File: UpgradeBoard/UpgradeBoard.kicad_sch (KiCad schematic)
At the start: 0 parts

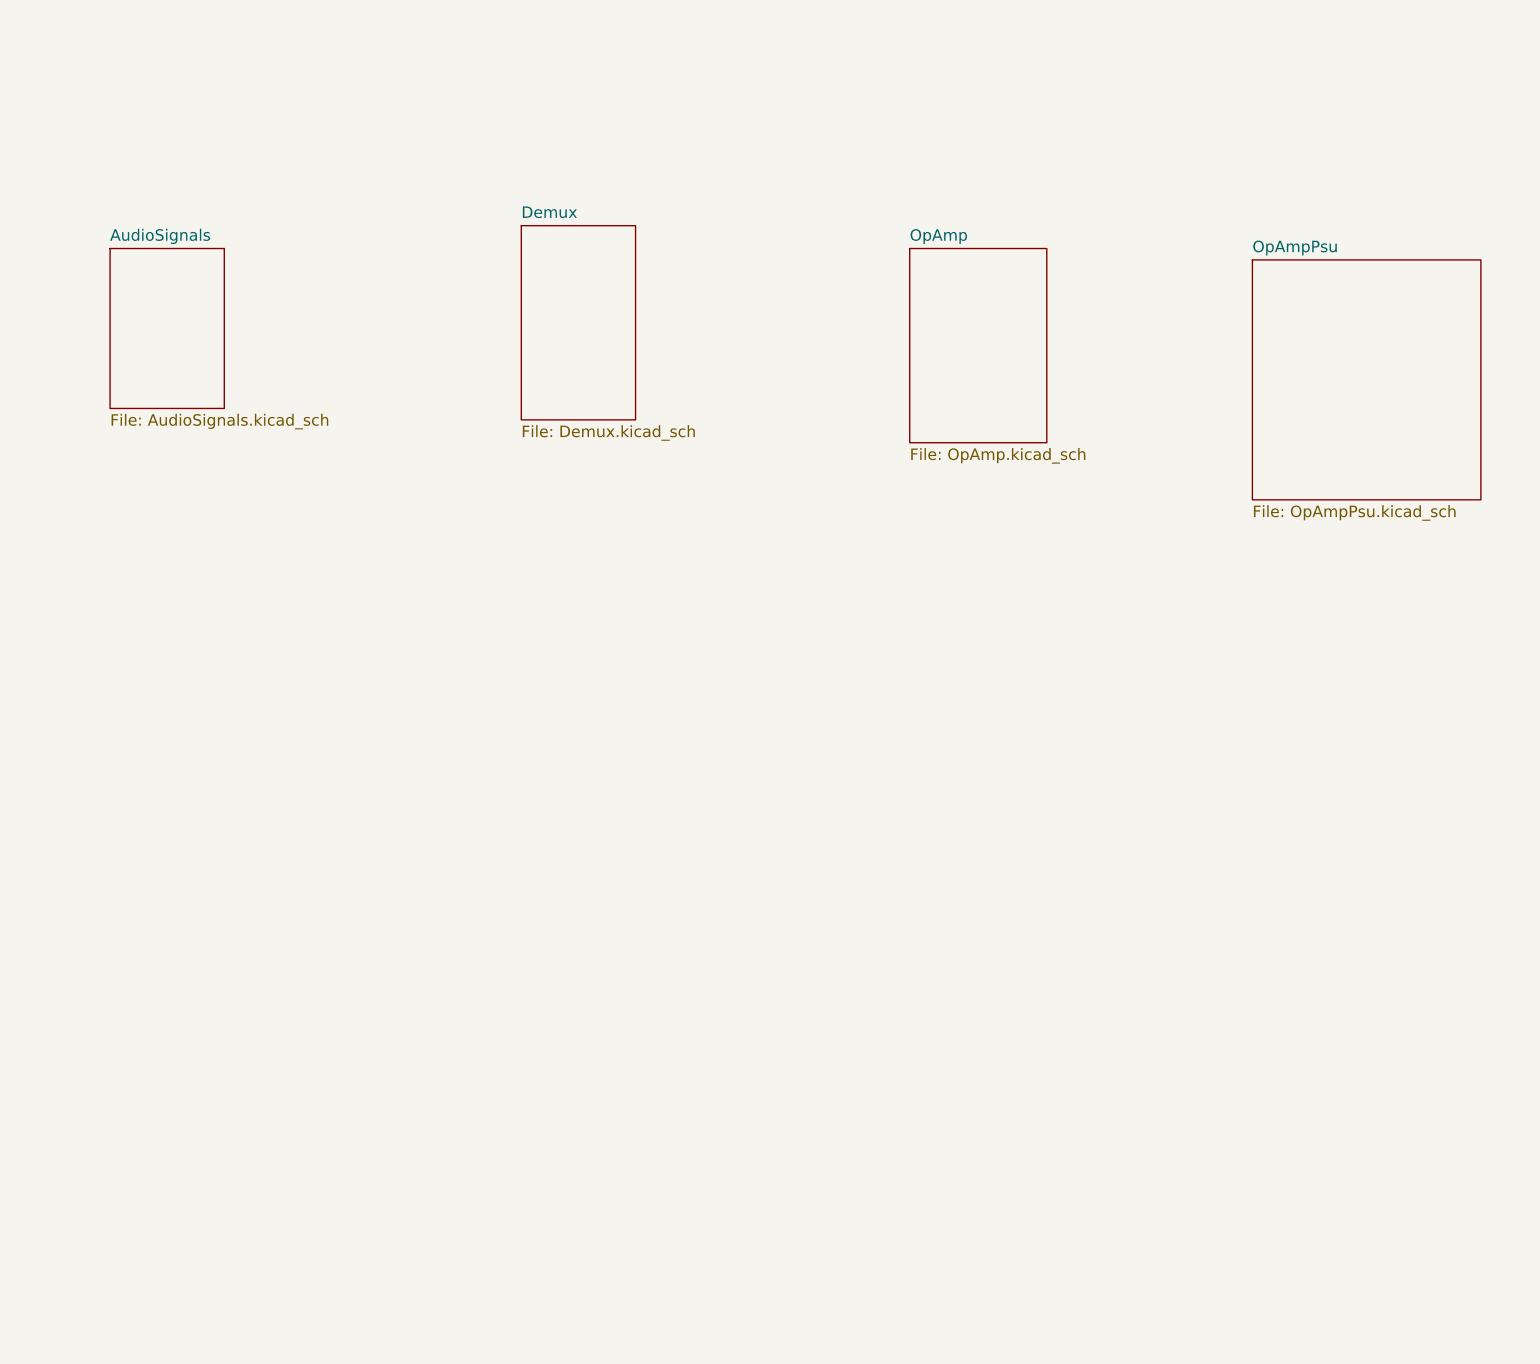
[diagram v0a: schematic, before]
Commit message: friday update
new hierarchical sheets, cabling, switching for main demux
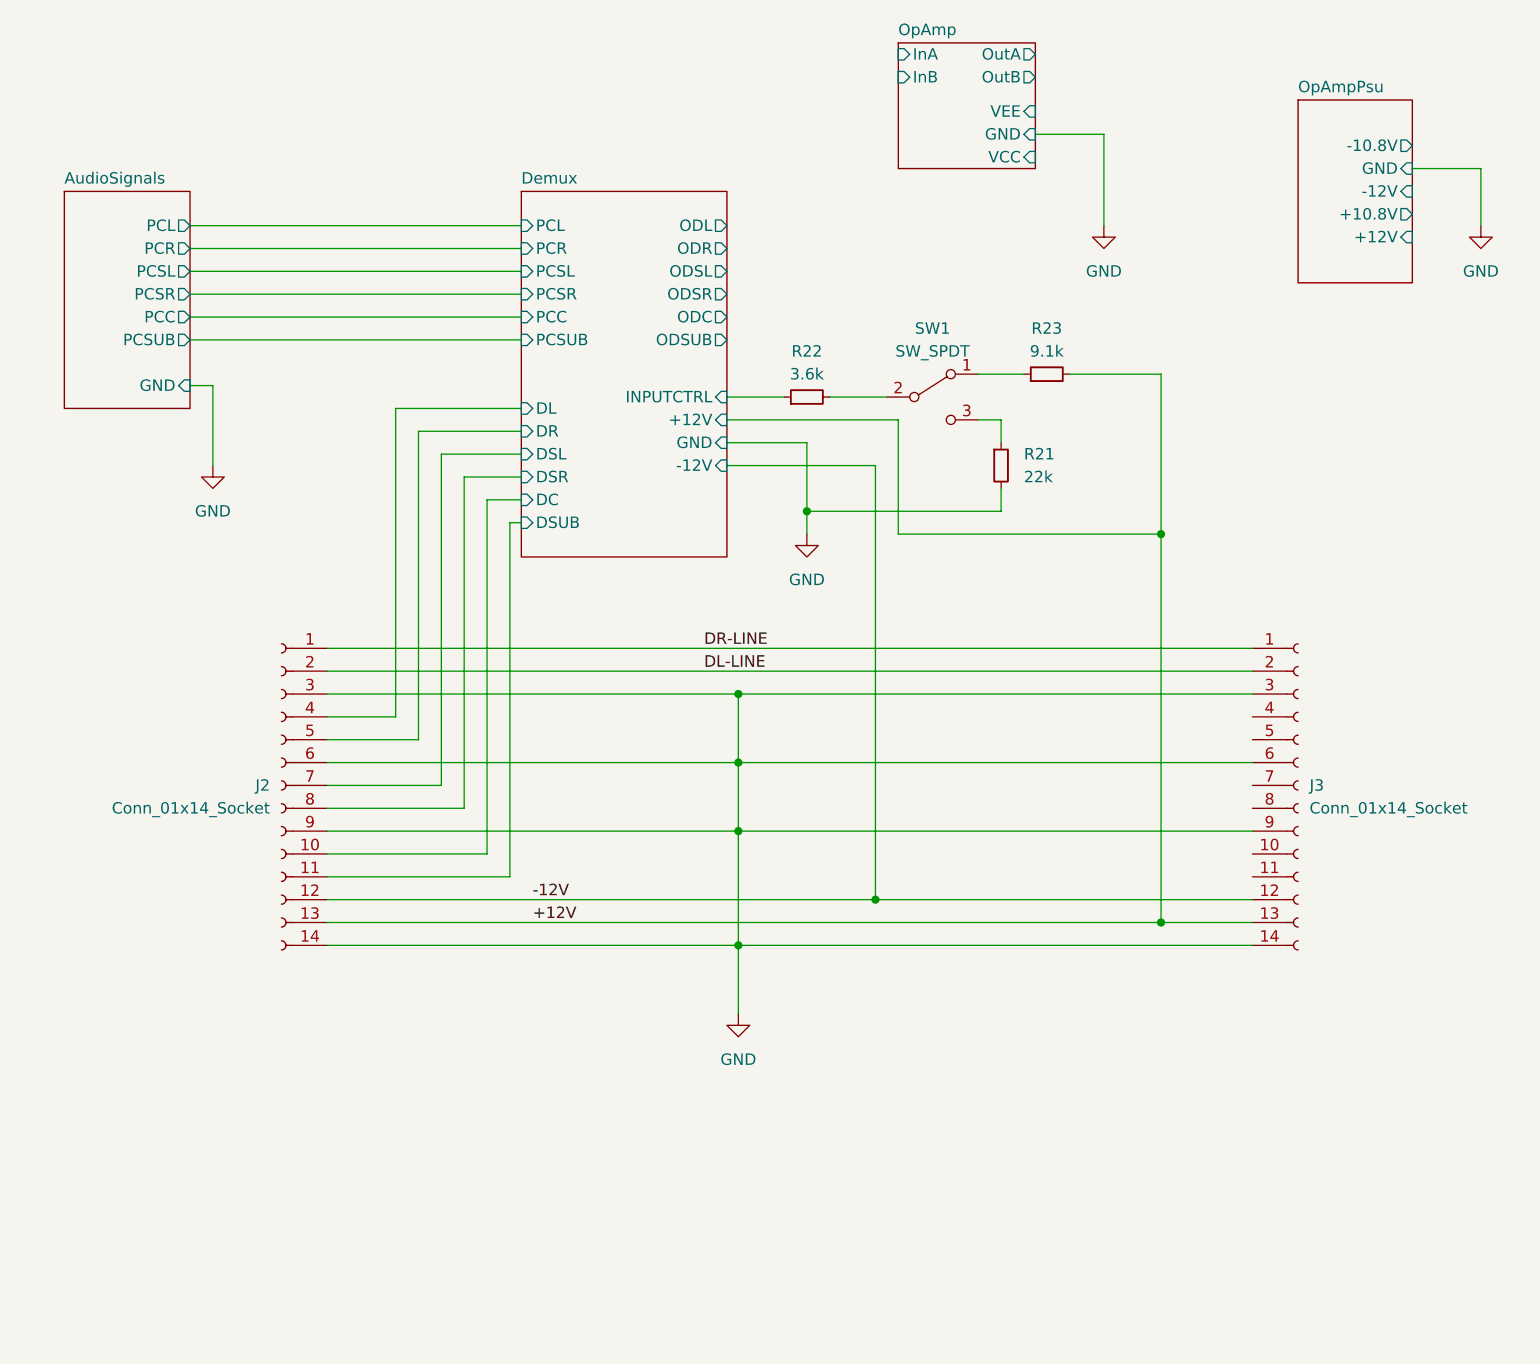
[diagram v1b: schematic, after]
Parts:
- added J2, J3: Conn_01x14_Socket, symbol Connector:Conn_01x14_Socket
- added R21: 22k, symbol Device:R_Small
- added R22: 3.6k, symbol Device:R_Small
- added R23: 9.1k, symbol Device:R_Small
- added SW1: SW_SPDT, symbol Switch:SW_SPDT
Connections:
- new net: R21.1, SW1.3 (C)
- new net: R23.1, SW1.1 (A)
- new net: R22.2, SW1.2 (B)
- new net +12V: J2.13 (Pin_13), J3.13 (Pin_13), R23.2
- new net -12V: J2.12 (Pin_12), J3.12 (Pin_12)
- new net DL-LINE: J2.2 (Pin_2), J3.2 (Pin_2)
- new net DR-LINE: J2.1 (Pin_1), J3.1 (Pin_1)
- new net Demux/DC: J2.10 (Pin_10)
- new net Demux/DL: J2.4 (Pin_4)
- new net Demux/DR: J2.5 (Pin_5)
- new net Demux/DSL: J2.7 (Pin_7)
- new net Demux/DSR: J2.8 (Pin_8)
- new net Demux/DSUB: J2.11 (Pin_11)
- new net Demux/INPUTCTRL: R22.1
- new net GND: J2.14 (Pin_14), J2.3 (Pin_3), J2.6 (Pin_6), J2.9 (Pin_9), J3.14 (Pin_14), J3.3 (Pin_3), J3.6 (Pin_6), J3.9 (Pin_9), R21.2
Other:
- sheet AudioSignals ports: added GND, PCC, PCL, PCR, PCSL, PCSR, PCSUB; removed none
- sheet Demux ports: added +12V, -12V, DC, DL, DR, DSL, DSR, DSUB, GND, INPUTCTRL, ODC, ODL, ODR, ODSL, ODSR, ODSUB, PCC, PCL, PCR, PCSL, PCSR, PCSUB; removed none
- sheet OpAmp ports: added GND, InA, InB, OutA, OutB, VCC, VEE; removed none
- sheet OpAmpPsu ports: added +10.8V, +12V, -10.8V, -12V, GND; removed none

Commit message: psucorrection
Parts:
- renumbered J2 to J1, J3 to J2, R22 to R1, R21 to R2, R23 to R3
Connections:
- net +12V: now also R3.1; no longer R3.2
- net Demux/ODC: now also J2.10 (Pin_10)
- net Demux/ODL: now also J2.4 (Pin_4)
- net Demux/ODR: now also J2.5 (Pin_5)
- net Demux/ODSL: now also J2.7 (Pin_7)
- net Demux/ODSR: now also J2.8 (Pin_8)
- net Demux/ODSUB: now also J2.11 (Pin_11)
- net GND: now also R2.1; no longer R2.2
- net at SW1.3 (C): now also R2.2; no longer R2.1
- net at SW1.1 (A): now also R3.2; no longer R3.1
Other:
- removed sheet OpAmp
- sheet AudioSignals ports: added VCC, VEE; removed none
- moved on the sheet: R2, R3, SW1

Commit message: updated components
added footprint and jlcpcb component number
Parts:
- R1: Desc (none) -> 3k6 5% 0,1W
- R2: Desc (none) -> 22k 5% 0,1W
- R3: Desc (none) -> 9K1 5% 0,1W
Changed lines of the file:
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@@
+      (effects (font (size 1.27 1.27)) hide)
+    )
+    (property "Desc" "22k 5% 0,1W" (at 165.1 73.66 90)
       (effects (font (size 1.27 1.27)) hide)
     )
@@
     )
     (property "Datasheet" "~" (at 173.99 73.66 0)
+      (effects (font (size 1.27 1.27)) hide)
+    )
+    (property "Desc" "9K1 5% 0,1W" (at 173.99 73.66 0)
       (effects (font (size 1.27 1.27)) hide)
     )
@@
       (effects (font (size 1.27 1.27)) hide)
     )
+    (property "Desc" "3k6 5% 0,1W" (at 153.67 62.23 90)
+      (effects (font (size 1.27 1.27)) hide)
+    )
     (pin "1")
     (pin "2")
@@
     (instances
       (project "UpgradeBoard"
-        (path "/32326095-4589-49eb-bfdc-5004b37213a0" (page "5"))
+        (path "/32326095-4589-49eb-bfdc-5004b37213a0" (page "10"))
       )
     )
@@
     (instances
       (project "UpgradeBoard"
-        (path "/32326095-4589-49eb-bfdc-5004b37213a0" (page "3"))
-      )
-    )
+        (path "/32326095-4589-49eb-bfdc-5004b37213a0" (page "9"))
+      )
+    )

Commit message: more components definition
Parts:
- J1, J2: footprint (none) -> Connector_FFC-FPC:Hirose_FH12-14S-0.5SH_1x14-1MP_P0.50mm_Horizontal
- R1, R2, R3: footprint (none) -> Resistor_SMD:R_0603_1608Metric
- SW1: footprint (none) -> Button_Switch_THT:SW_CuK_OS102011MA1QN1_SPDT_Angled
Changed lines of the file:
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@@
       (effects (font (size 1.27 1.27)) (justify left))
     )
-    (property "Footprint" "" (at 208.28 105.41 0)
+    (property "Footprint" "Connector_FFC-FPC:Hirose_FH12-14S-0.5SH_1x14-1MP_P0.50mm_Horizontal" (at 208.28 105.41 0)
       (effects (font (size 1.27 1.27)) hide)
     )
@@
       (effects (font (size 1.27 1.27)))
     )
-    (property "Footprint" "" (at 165.1 73.66 0)
+    (property "Footprint" "Resistor_SMD:R_0603_1608Metric" (at 165.1 73.66 0)
       (effects (font (size 1.27 1.27)) hide)
     )
@@
       (effects (font (size 1.27 1.27)) (justify right))
     )
-    (property "Footprint" "" (at 173.99 73.66 0)
+    (property "Footprint" "Resistor_SMD:R_0603_1608Metric" (at 173.99 73.66 0)
       (effects (font (size 1.27 1.27)) hide)
     )
@@
       (effects (font (size 1.27 1.27)) (justify left))
     )
-    (property "Footprint" "" (at 95.25 105.41 0)
+    (property "Footprint" "Connector_FFC-FPC:Hirose_FH12-14S-0.5SH_1x14-1MP_P0.50mm_Horizontal" (at 95.25 105.41 0)
       (effects (font (size 1.27 1.27)) hide)
     )
@@
       (effects (font (size 1.27 1.27)) (justify left))
     )
-    (property "Footprint" "" (at 171.45 64.77 0)
+    (property "Footprint" "Button_Switch_THT:SW_CuK_OS102011MA1QN1_SPDT_Angled" (at 171.45 64.77 0)
       (effects (font (size 1.27 1.27)) hide)
     )
@@
       (effects (font (size 1.27 1.27)))
     )
-    (property "Footprint" "" (at 153.67 62.23 0)
-      (effects (font (size 1.27 1.27)) hide)
-    )
+    (property "Footprint" "Resistor_SMD:R_0603_1608Metric" (at 153.67 62.23 0)
+      (effects (font (size 1.27 1.27)) hide)
+    )
